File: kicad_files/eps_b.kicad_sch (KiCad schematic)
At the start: 34 parts, among them J12 5051101592, Q3 TEMT6000X01, U15 MCP3427-xUN, U16 BQ25570

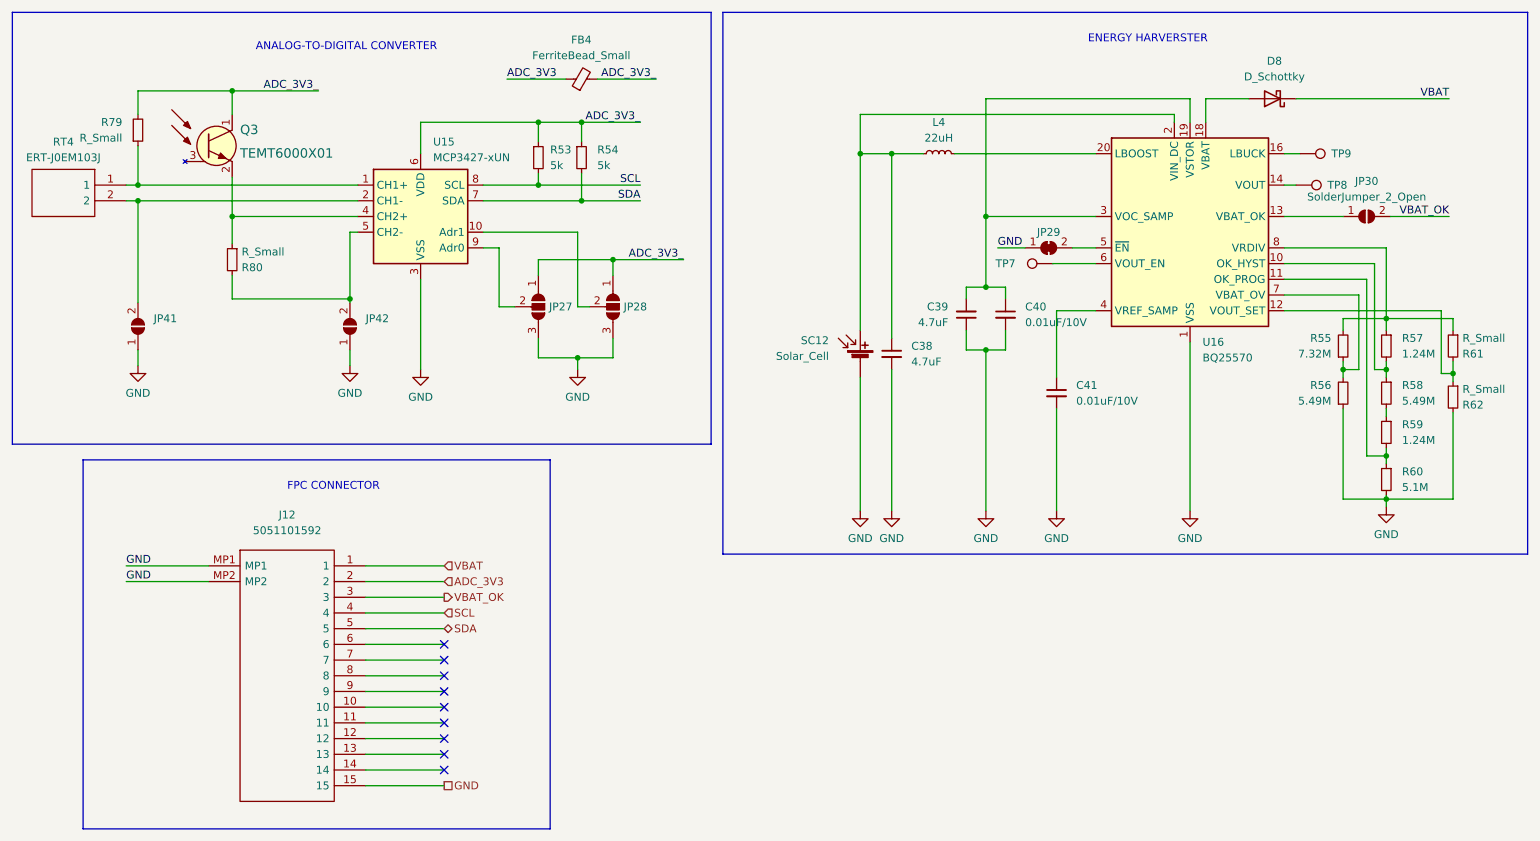
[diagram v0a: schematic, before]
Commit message: update components values
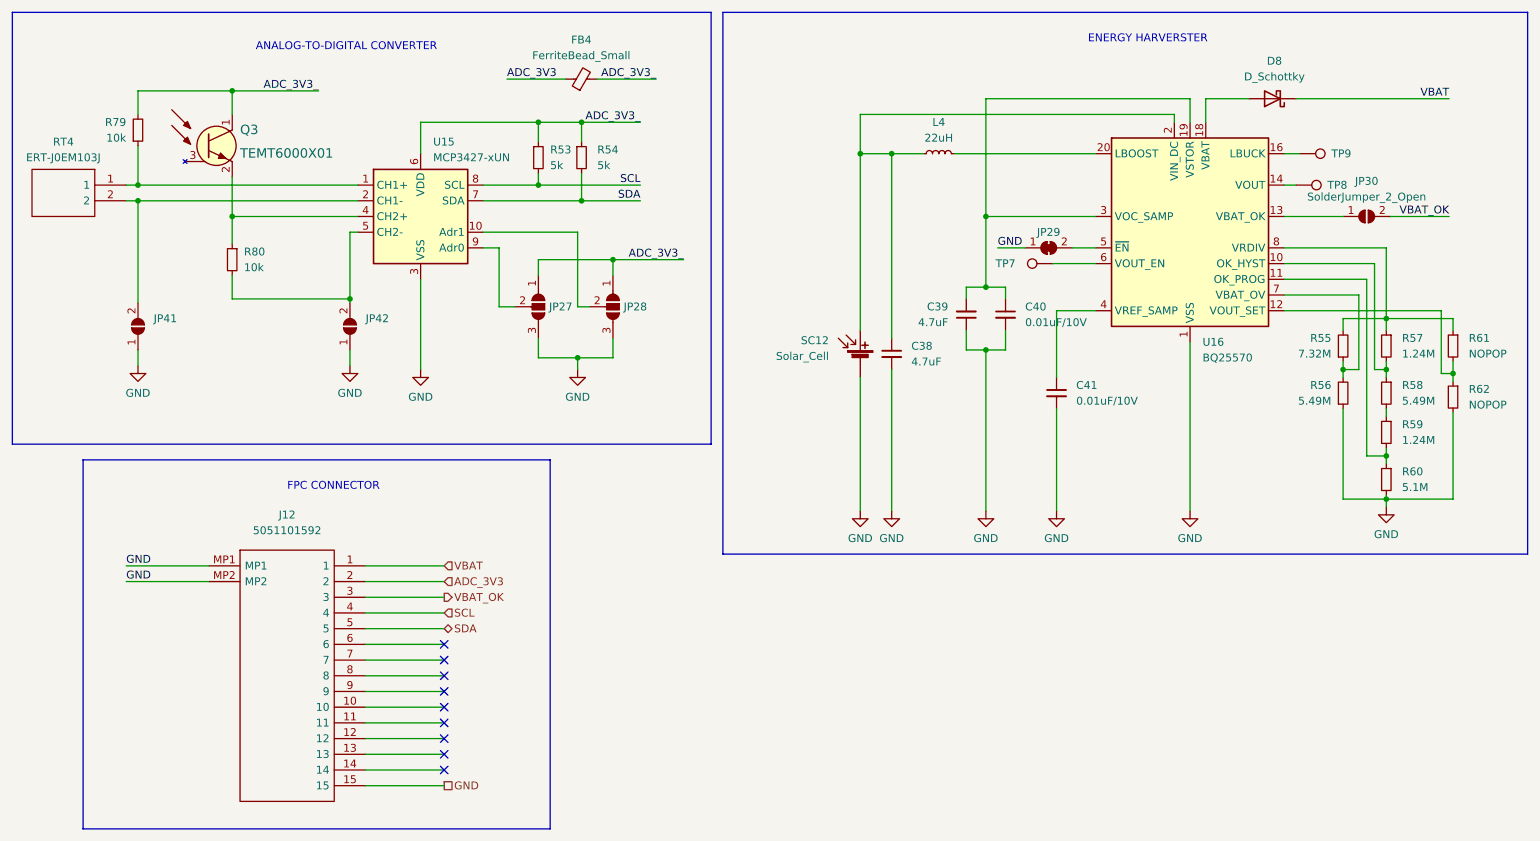
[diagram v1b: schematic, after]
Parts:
- R61, R62: value R_Small -> NOPOP
- R79, R80: value R_Small -> 10k
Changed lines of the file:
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@@
   (symbol (lib_id "Device:R_Small") (at 257.81 104.775 0) (mirror y) (unit 1)
     (in_bom yes) (on_board yes) (fields_autoplaced)
-    (property "Reference" "R62" (id 0) (at 259.334 106.0451 0)
-      (effects (font (size 1.27 1.27)) (justify right))
-    )
-    (property "Value" "R_Small" (id 1) (at 259.334 103.5051 0)
+    (property "Reference" "R62" (id 0) (at 260.35 103.5049 0)
+      (effects (font (size 1.27 1.27)) (justify right))
+    )
+    (property "Value" "NOPOP" (id 1) (at 260.35 106.0449 0)
       (effects (font (size 1.27 1.27)) (justify right))
     )
@@
   (symbol (lib_id "Device:R_Small") (at 45.085 61.595 0) (mirror x) (unit 1)
     (in_bom yes) (on_board yes) (fields_autoplaced)
-    (property "Reference" "R79" (id 0) (at 42.545 60.3249 0)
-      (effects (font (size 1.27 1.27)) (justify right))
-    )
-    (property "Value" "R_Small" (id 1) (at 42.545 62.8649 0)
+    (property "Reference" "R79" (id 0) (at 43.18 60.3249 0)
+      (effects (font (size 1.27 1.27)) (justify right))
+    )
+    (property "Value" "10k" (id 1) (at 43.18 62.8649 0)
       (effects (font (size 1.27 1.27)) (justify right))
     )
@@
   (symbol (lib_id "Device:R_Small") (at 60.325 82.55 0) (mirror y) (unit 1)
     (in_bom yes) (on_board yes) (fields_autoplaced)
-    (property "Reference" "R80" (id 0) (at 61.849 83.8201 0)
-      (effects (font (size 1.27 1.27)) (justify right))
-    )
-    (property "Value" "R_Small" (id 1) (at 61.849 81.2801 0)
+    (property "Reference" "R80" (id 0) (at 62.23 81.2799 0)
+      (effects (font (size 1.27 1.27)) (justify right))
+    )
+    (property "Value" "10k" (id 1) (at 62.23 83.8199 0)
       (effects (font (size 1.27 1.27)) (justify right))
     )
@@
   (symbol (lib_id "Device:R_Small") (at 257.81 96.52 0) (mirror y) (unit 1)
     (in_bom yes) (on_board yes) (fields_autoplaced)
-    (property "Reference" "R61" (id 0) (at 259.334 97.7901 0)
-      (effects (font (size 1.27 1.27)) (justify right))
-    )
-    (property "Value" "R_Small" (id 1) (at 259.334 95.2501 0)
-      (effects (font (size 1.27 1.27)) (justify right))
-    )
+    (property "Reference" "R61" (id 0) (at 260.35 95.2499 0)
+      (effects (font (size 1.27 1.27)) (justify right))
+    )
+    (property "Value" "NOPOP" (id 1) (at 260.35 97.7899 0)
+      (effects (font (size 1.27 1.27)) (justify right))
+    )
